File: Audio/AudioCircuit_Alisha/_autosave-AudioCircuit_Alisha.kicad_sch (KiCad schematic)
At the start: 17 parts, among them J1 Conn_01x02_Pin, J2 PWM_VOL, J3 226Hz, U1 LM4875M, U4 TLV172IDCK

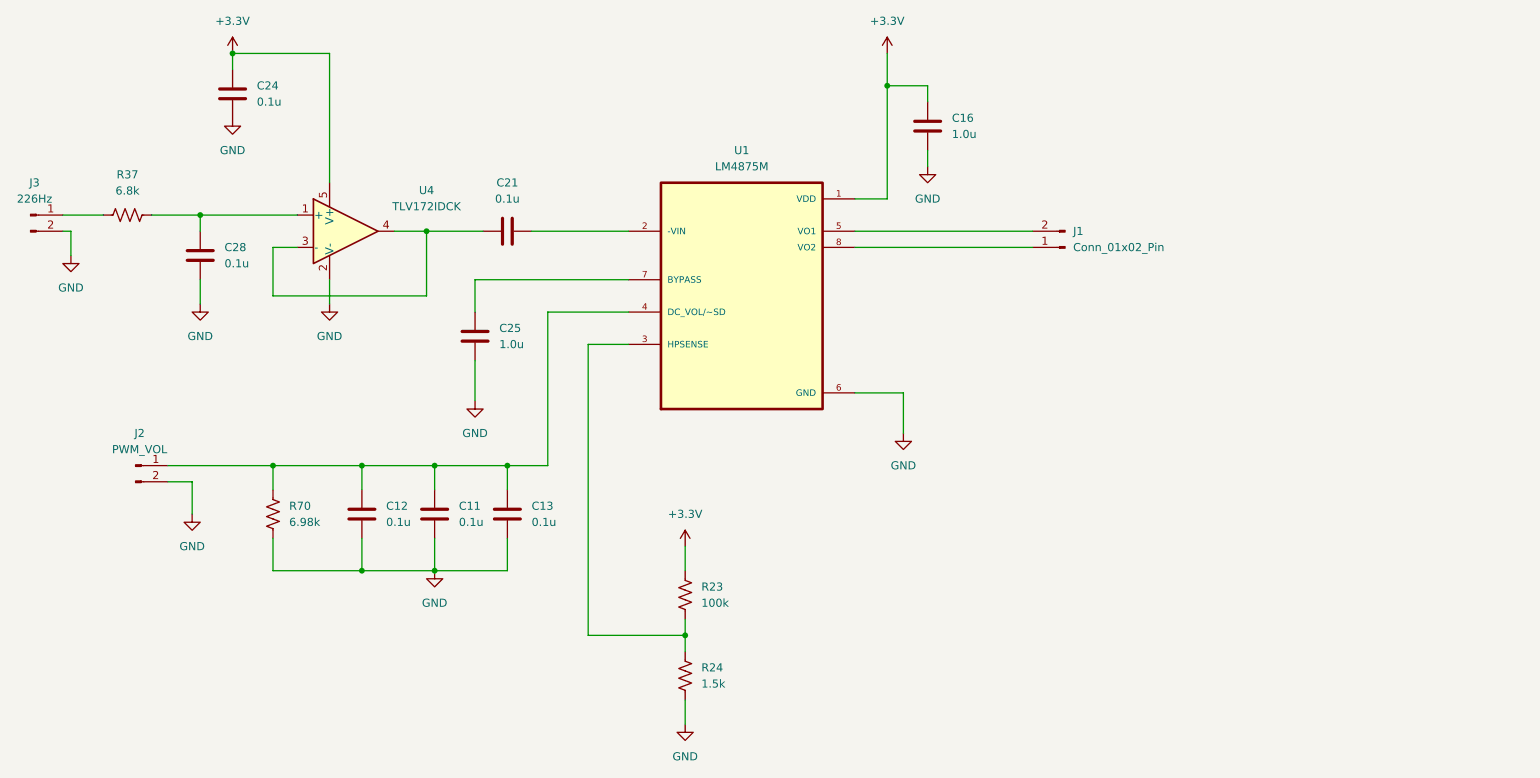
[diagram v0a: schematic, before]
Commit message: audio pcb added footprints, arduino board, and copper
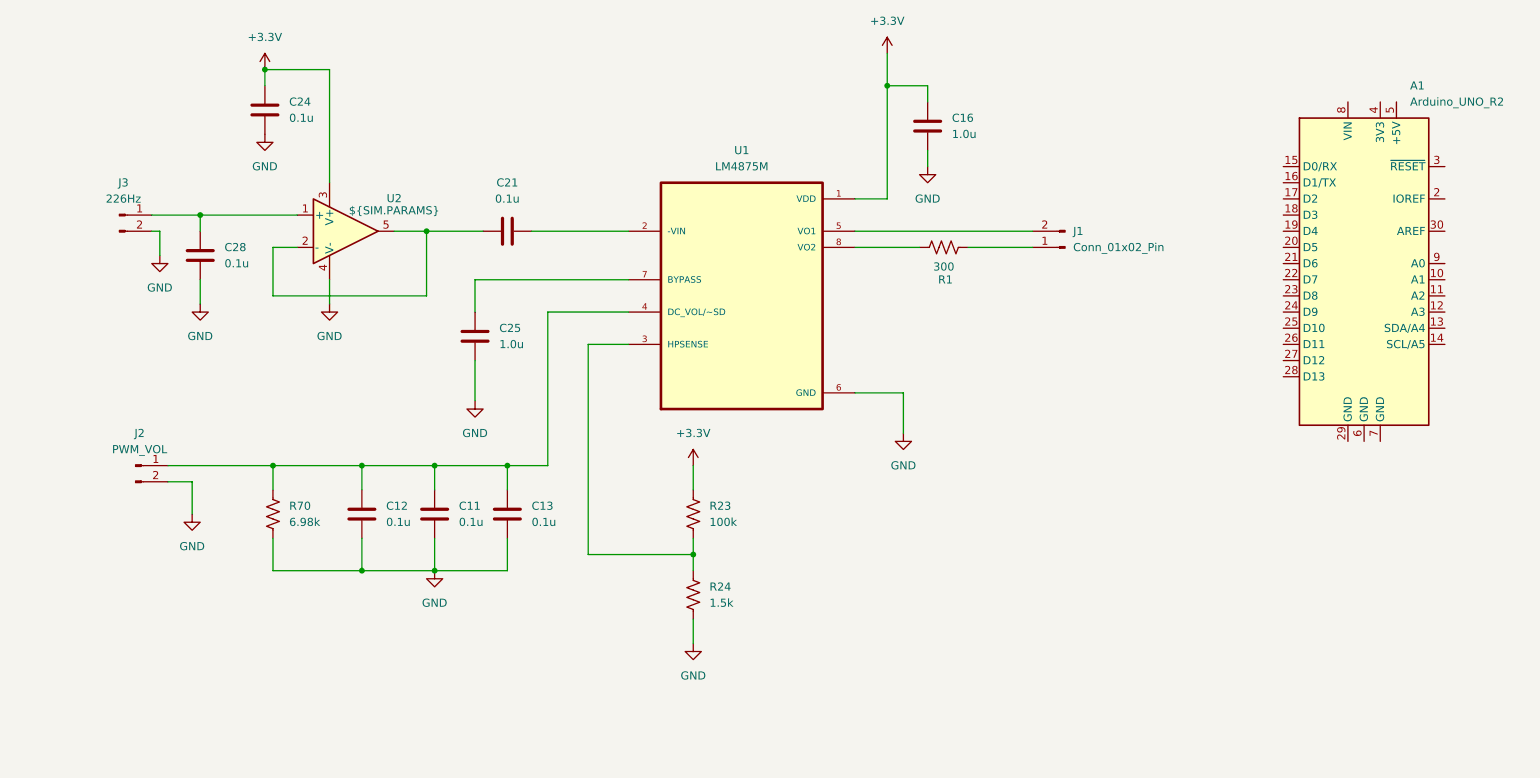
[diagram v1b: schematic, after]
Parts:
- removed R37: 6.8k, Inductor_SMD:L_Changjiang_FTC160808S, symbol Device:R_US
- removed U4: TLV172IDCK, OP_AMP:DBV5_TEX-M, symbol Amplifier_Operational:TLV172IDCK
- added A1: Arduino_UNO_R2, Module:Arduino_UNO_R2, symbol MCU_Module:Arduino_UNO_R2
- added R1: 300, Inductor_SMD:L_Changjiang_FTC160808S, symbol Device:R_US
- added U2: ${SIM.PARAMS}, OP_AMP:DBV5_TEX-M, symbol Simulation_SPICE:OPAMP
- C11, C12, C13, C16, C21, C24, C25, C28: footprint C0603C104K5RACTU:CAPC1608X90 -> (none)
- J1, J2, J3: footprint Connector_PinHeader_2.54mm:PinHeader_1x02_P2.54mm_Vertical -> (none)
- R23, R24, R70: footprint Inductor_SMD:L_Changjiang_FTC160808S -> (none)
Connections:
- net +3.3V: now also U2.3 (V+)
- net GND: now also U2.4 (V-)
- net at J3.1 (Pin_1): now also C28.1, U2.1 (+)
- net at U1.8 (VO2): now also R1.1; no longer J1.1 (Pin_1)
- net at C21.1: now also U2.2 (-), U2.5
- new net: J1.1 (Pin_1), R1.2
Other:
- moved on the sheet: C24, J3, R23, R24
